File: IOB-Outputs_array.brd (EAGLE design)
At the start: 104.1 x 106.7 mm, 65 parts

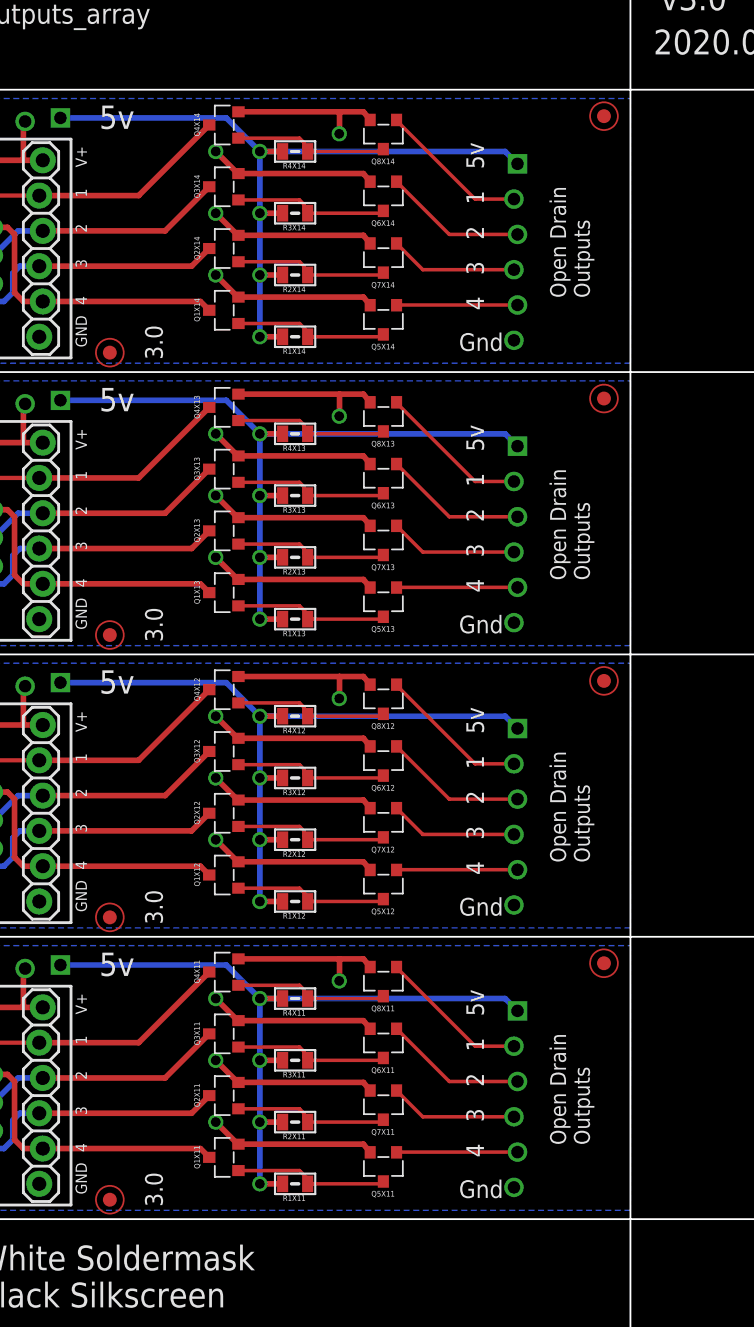
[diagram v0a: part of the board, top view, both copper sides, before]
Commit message: fixed SPCoast.lbr diode orientation
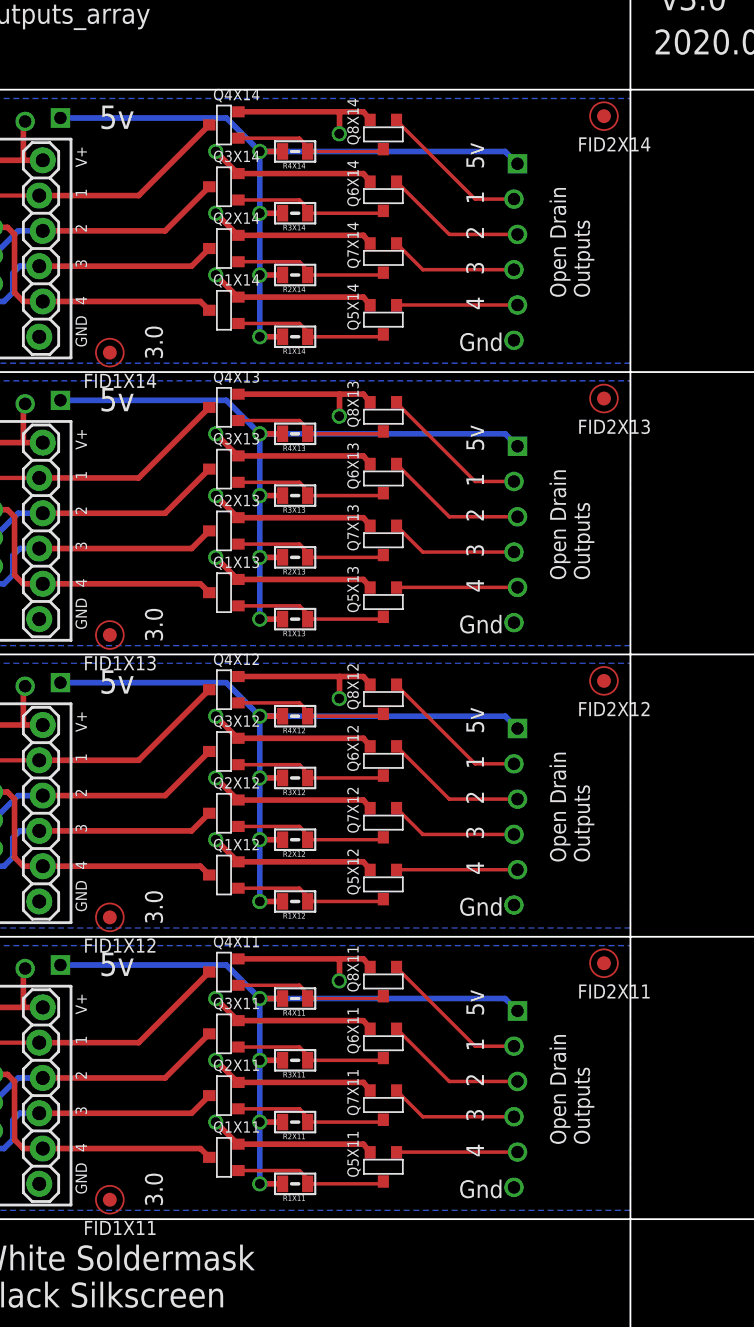
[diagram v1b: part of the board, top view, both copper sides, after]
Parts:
- turned Q1X11 to 0 degrees
- turned Q1X12 to 0 degrees
- turned Q1X13 to 0 degrees
- turned Q1X14 to 0 degrees
- turned Q2X11 to 0 degrees
- turned Q2X12 to 0 degrees
- turned Q2X13 to 0 degrees
- turned Q2X14 to 0 degrees
- turned Q3X11 to 0 degrees
- turned Q3X12 to 0 degrees
- turned Q3X13 to 0 degrees
- turned Q3X14 to 0 degrees
- turned Q4X11 to 0 degrees
- turned Q4X12 to 0 degrees
- turned Q4X13 to 0 degrees
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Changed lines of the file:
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@@
 <element name="FID1X11" library="SPCoast" package="FIDUCIAL_1MM" value="" x="41.275" y="10.287"/>
 <element name="FID2X11" library="SPCoast" package="FIDUCIAL_1MM" value="" x="76.835" y="27.305"/>
-<element name="Q1X11" library="SPCoast" package="SOT23-3" value="" x="49.53" y="13.335" rot="R90"/>
-<element name="Q2X11" library="SPCoast" package="SOT23-3" value="" x="49.53" y="17.78" rot="R90"/>
-<element name="Q3X11" library="SPCoast" package="SOT23-3" value="" x="49.53" y="22.225" rot="R90"/>
-<element name="Q4X11" library="SPCoast" package="SOT23-3" value="" x="49.53" y="26.67" rot="R90"/>
-<element name="Q5X11" library="SPCoast" package="SOT23-3" value="" x="60.96" y="12.7" rot="R180"/>
-<element name="Q6X11" library="SPCoast" package="SOT23-3" value="" x="60.96" y="21.59" rot="R180"/>
-<element name="Q7X11" library="SPCoast" package="SOT23-3" value="" x="60.96" y="17.145" rot="R180"/>
-<element name="Q8X11" library="SPCoast" package="SOT23-3" value="" x="60.96" y="26.035" rot="R180"/>
+<element name="Q1X11" library="SPCoast" package="SOT23-3" value="" x="49.53" y="13.335"/>
+<element name="Q2X11" library="SPCoast" package="SOT23-3" value="" x="49.53" y="17.78"/>
+<element name="Q3X11" library="SPCoast" package="SOT23-3" value="" x="49.53" y="22.225"/>
+<element name="Q4X11" library="SPCoast" package="SOT23-3" value="" x="49.53" y="26.67"/>
+<element name="Q5X11" library="SPCoast" package="SOT23-3" value="" x="60.96" y="12.7" rot="R90"/>
+<element name="Q6X11" library="SPCoast" package="SOT23-3" value="" x="60.96" y="21.59" rot="R90"/>
+<element name="Q7X11" library="SPCoast" package="SOT23-3" value="" x="60.96" y="17.145" rot="R90"/>
+<element name="Q8X11" library="SPCoast" package="SOT23-3" value="" x="60.96" y="26.035" rot="R90"/>
 <element name="R1X11" library="SPCoast" package="0805-RES" value="" x="54.61" y="11.43" rot="R180"/>
 <element name="R2X11" library="SPCoast" package="0805-RES" value="" x="54.61" y="15.875" rot="R180"/>
@@
 <element name="FID1X12" library="SPCoast" package="FIDUCIAL_1MM" value="" x="41.275" y="30.607"/>
 <element name="FID2X12" library="SPCoast" package="FIDUCIAL_1MM" value="" x="76.835" y="47.625"/>
-<element name="Q1X12" library="SPCoast" package="SOT23-3" value="" x="49.53" y="33.655" rot="R90"/>
-<element name="Q2X12" library="SPCoast" package="SOT23-3" value="" x="49.53" y="38.1" rot="R90"/>
-<element name="Q3X12" library="SPCoast" package="SOT23-3" value="" x="49.53" y="42.545" rot="R90"/>
-<element name="Q4X12" library="SPCoast" package="SOT23-3" value="" x="49.53" y="46.99" rot="R90"/>
-<element name="Q5X12" library="SPCoast" package="SOT23-3" value="" x="60.96" y="33.02" rot="R180"/>
-<element name="Q6X12" library="SPCoast" package="SOT23-3" value="" x="60.96" y="41.91" rot="R180"/>
-<element name="Q7X12" library="SPCoast" package="SOT23-3" value="" x="60.96" y="37.465" rot="R180"/>
-<element name="Q8X12" library="SPCoast" package="SOT23-3" value="" x="60.96" y="46.355" rot="R180"/>
+<element name="Q1X12" library="SPCoast" package="SOT23-3" value="" x="49.53" y="33.655"/>
+<element name="Q2X12" library="SPCoast" package="SOT23-3" value="" x="49.53" y="38.1"/>
+<element name="Q3X12" library="SPCoast" package="SOT23-3" value="" x="49.53" y="42.545"/>
+<element name="Q4X12" library="SPCoast" package="SOT23-3" value="" x="49.53" y="46.99"/>
+<element name="Q5X12" library="SPCoast" package="SOT23-3" value="" x="60.96" y="33.02" rot="R90"/>
+<element name="Q6X12" library="SPCoast" package="SOT23-3" value="" x="60.96" y="41.91" rot="R90"/>
+<element name="Q7X12" library="SPCoast" package="SOT23-3" value="" x="60.96" y="37.465" rot="R90"/>
+<element name="Q8X12" library="SPCoast" package="SOT23-3" value="" x="60.96" y="46.355" rot="R90"/>
 <element name="R1X12" library="SPCoast" package="0805-RES" value="" x="54.61" y="31.75" rot="R180"/>
 <element name="R2X12" library="SPCoast" package="0805-RES" value="" x="54.61" y="36.195" rot="R180"/>
@@
 <element name="FID1X13" library="SPCoast" package="FIDUCIAL_1MM" value="" x="41.275" y="50.927"/>
 <element name="FID2X13" library="SPCoast" package="FIDUCIAL_1MM" value="" x="76.835" y="67.945"/>
-<element name="Q1X13" library="SPCoast" package="SOT23-3" value="" x="49.53" y="53.975" rot="R90"/>
-<element name="Q2X13" library="SPCoast" package="SOT23-3" value="" x="49.53" y="58.42" rot="R90"/>
-<element name="Q3X13" library="SPCoast" package="SOT23-3" value="" x="49.53" y="62.865" rot="R90"/>
-<element name="Q4X13" library="SPCoast" package="SOT23-3" value="" x="49.53" y="67.31" rot="R90"/>
-<element name="Q5X13" library="SPCoast" package="SOT23-3" value="" x="60.96" y="53.34" rot="R180"/>
-<element name="Q6X13" library="SPCoast" package="SOT23-3" value="" x="60.96" y="62.23" rot="R180"/>
-<element name="Q7X13" library="SPCoast" package="SOT23-3" value="" x="60.96" y="57.785" rot="R180"/>
-<element name="Q8X13" library="SPCoast" package="SOT23-3" value="" x="60.96" y="66.675" rot="R180"/>
+<element name="Q1X13" library="SPCoast" package="SOT23-3" value="" x="49.53" y="53.975"/>
+<element name="Q2X13" library="SPCoast" package="SOT23-3" value="" x="49.53" y="58.42"/>
+<element name="Q3X13" library="SPCoast" package="SOT23-3" value="" x="49.53" y="62.865"/>
+<element name="Q4X13" library="SPCoast" package="SOT23-3" value="" x="49.53" y="67.31"/>
+<element name="Q5X13" library="SPCoast" package="SOT23-3" value="" x="60.96" y="53.34" rot="R90"/>
+<element name="Q6X13" library="SPCoast" package="SOT23-3" value="" x="60.96" y="62.23" rot="R90"/>
+<element name="Q7X13" library="SPCoast" package="SOT23-3" value="" x="60.96" y="57.785" rot="R90"/>
+<element name="Q8X13" library="SPCoast" package="SOT23-3" value="" x="60.96" y="66.675" rot="R90"/>
 <element name="R1X13" library="SPCoast" package="0805-RES" value="" x="54.61" y="52.07" rot="R180"/>
 <element name="R2X13" library="SPCoast" package="0805-RES" value="" x="54.61" y="56.515" rot="R180"/>
@@
 <element name="FID1X14" library="SPCoast" package="FIDUCIAL_1MM" value="" x="41.275" y="71.247"/>
 <element name="FID2X14" library="SPCoast" package="FIDUCIAL_1MM" value="" x="76.835" y="88.265"/>
-<element name="Q1X14" library="SPCoast" package="SOT23-3" value="" x="49.53" y="74.295" rot="R90"/>
-<element name="Q2X14" library="SPCoast" package="SOT23-3" value="" x="49.53" y="78.74" rot="R90"/>
-<element name="Q3X14" library="SPCoast" package="SOT23-3" value="" x="49.53" y="83.185" rot="R90"/>
-<element name="Q4X14" library="SPCoast" package="SOT23-3" value="" x="49.53" y="87.63" rot="R90"/>
-<element name="Q5X14" library="SPCoast" package="SOT23-3" value="" x="60.96" y="73.66" rot="R180"/>
-<element name="Q6X14" library="SPCoast" package="SOT23-3" value="" x="60.96" y="82.55" rot="R180"/>
-<element name="Q7X14" library="SPCoast" package="SOT23-3" value="" x="60.96" y="78.105" rot="R180"/>
-<element name="Q8X14" library="SPCoast" package="SOT23-3" value="" x="60.96" y="86.995" rot="R180"/>
+<element name="Q1X14" library="SPCoast" package="SOT23-3" value="" x="49.53" y="74.295"/>
+<element name="Q2X14" library="SPCoast" package="SOT23-3" value="" x="49.53" y="78.74"/>
+<element name="Q3X14" library="SPCoast" package="SOT23-3" value="" x="49.53" y="83.185"/>
+<element name="Q4X14" library="SPCoast" package="SOT23-3" value="" x="49.53" y="87.63"/>
+<element name="Q5X14" library="SPCoast" package="SOT23-3" value="" x="60.96" y="73.66" rot="R90"/>
+<element name="Q6X14" library="SPCoast" package="SOT23-3" value="" x="60.96" y="82.55" rot="R90"/>
+<element name="Q7X14" library="SPCoast" package="SOT23-3" value="" x="60.96" y="78.105" rot="R90"/>
+<element name="Q8X14" library="SPCoast" package="SOT23-3" value="" x="60.96" y="86.995" rot="R90"/>
 <element name="R1X14" library="SPCoast" package="0805-RES" value="" x="54.61" y="72.39" rot="R180"/>
 <element name="R2X14" library="SPCoast" package="0805-RES" value="" x="54.61" y="76.835" rot="R180"/>

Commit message: Added missing values
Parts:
- Q1X11, Q1X12, Q1X13, Q1X14, Q2X11, Q2X12, Q2X13, Q2X14, Q3X11, Q3X12, Q3X13, Q3X14, Q4X11, Q4X12, Q4X13, Q4X14, Q5X11, Q5X12, Q5X13, Q5X14, Q6X11, Q6X12, Q6X13, Q6X14, Q7X11, Q7X12, Q7X13, Q7X14, Q8X11, Q8X12, Q8X13, Q8X14: value (none) -> MOSFET-N
- R1X11, R1X12, R1X13, R1X14, R2X11, R2X12, R2X13, R2X14, R3X11, R3X12, R3X13, R3X14, R4X11, R4X12, R4X13, R4X14: value (none) -> 10k

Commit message: normalized silkscreen layout across IOBs
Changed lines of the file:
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@@
 <plain>
 <text x="27.94" y="14.351" size="1.27" layer="21" font="vector" rot="R90">IO4-IOB</text>
-<text x="45.085" y="9.779" size="1.27" layer="21" font="vector" rot="R90">3.0</text>
+<text x="77.47" y="9.779" size="1.27" layer="21" font="vector" rot="R90">3.0</text>
 <text x="75.819" y="14.224" size="1.143" layer="21" font="vector" rot="R90">Open Drain
 Outputs</text>
@@
 <text x="55.626" y="26.9875" size="1.016" layer="125" font="vector" rot="R180">R4</text>
 <text x="27.94" y="34.671" size="1.27" layer="21" font="vector" rot="R90">IO4-IOB</text>
-<text x="45.085" y="30.099" size="1.27" layer="21" font="vector" rot="R90">3.0</text>
+<text x="77.47" y="30.099" size="1.27" layer="21" font="vector" rot="R90">3.0</text>
 <text x="75.819" y="34.544" size="1.143" layer="21" font="vector" rot="R90">Open Drain
 Outputs</text>
@@
 <text x="55.626" y="47.3075" size="1.016" layer="125" font="vector" rot="R180">R4</text>
 <text x="27.94" y="54.991" size="1.27" layer="21" font="vector" rot="R90">IO4-IOB</text>
-<text x="45.085" y="50.419" size="1.27" layer="21" font="vector" rot="R90">3.0</text>
+<text x="77.47" y="50.419" size="1.27" layer="21" font="vector" rot="R90">3.0</text>
 <text x="75.819" y="54.864" size="1.143" layer="21" font="vector" rot="R90">Open Drain
 Outputs</text>
@@
 <text x="55.626" y="67.6275" size="1.016" layer="125" font="vector" rot="R180">R4</text>
 <text x="27.94" y="75.311" size="1.27" layer="21" font="vector" rot="R90">IO4-IOB</text>
-<text x="45.085" y="70.739" size="1.27" layer="21" font="vector" rot="R90">3.0</text>
+<text x="77.47" y="70.739" size="1.27" layer="21" font="vector" rot="R90">3.0</text>
 <text x="75.819" y="75.184" size="1.143" layer="21" font="vector" rot="R90">Open Drain
 Outputs</text>

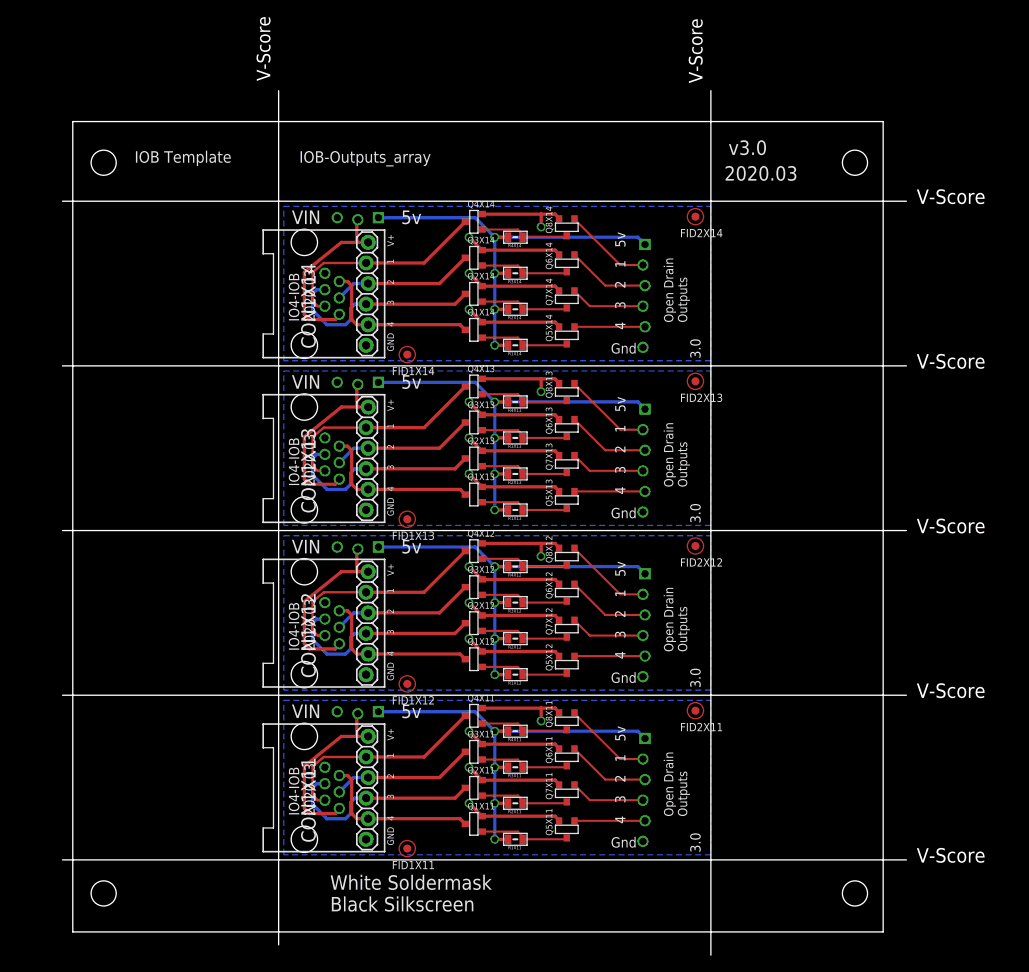
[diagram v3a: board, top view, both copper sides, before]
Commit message: move text from DOCU to TPLACE
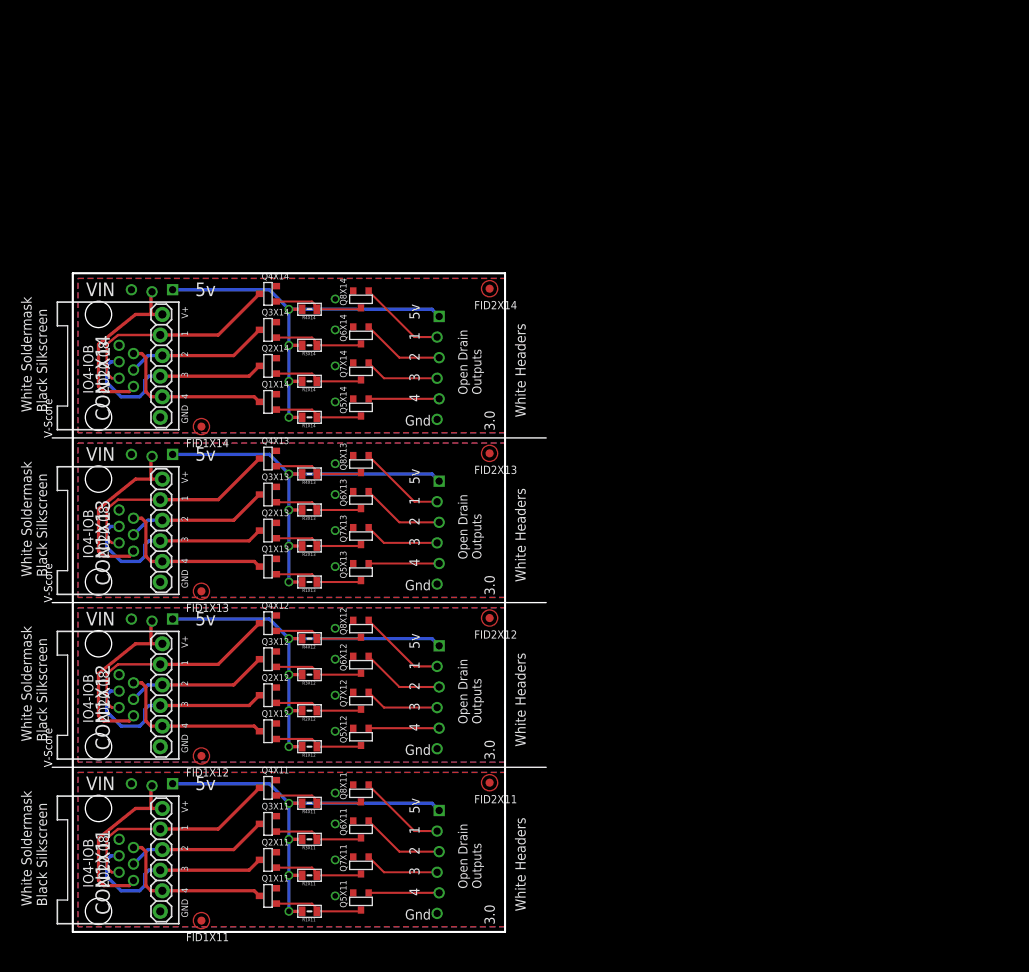
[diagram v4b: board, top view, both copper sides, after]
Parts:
- removed U$1X1: (no value), SPCoast:BOARD-DINRAIL-3.17IN-H4X-IOB
- FID1X11, FID1X12, FID1X13, FID1X14, FID2X11, FID2X12, FID2X13, FID2X14: value (none) -> FIDUCIAL
- U$1X11, U$1X12, U$1X13, U$1X14: value (none) -> CONNECTOR-IO4-IOBFULL
- moved Q1X11 26.9 mm to (24.1, 4.45)
- moved Q1X12 26.9 mm to (24.1, 24.8)
- moved Q1X13 26.9 mm to (24.1, 45.1)
- moved Q1X14 26.9 mm to (24.1, 65.4)
- moved Q2X11 26.9 mm to (24.1, 8.89)
- moved Q2X12 26.9 mm to (24.1, 29.2)
- moved Q2X13 26.9 mm to (24.1, 49.5)
- moved Q2X14 26.9 mm to (24.1, 69.8)
- moved Q3X11 26.9 mm to (24.1, 13.3)
- moved Q3X12 26.9 mm to (24.1, 33.7)
- moved Q3X13 26.9 mm to (24.1, 54.0)
- moved Q3X14 26.9 mm to (24.1, 74.3)
- moved Q4X11 26.9 mm to (24.1, 17.8)
- moved Q4X12 26.9 mm to (24.1, 38.1)
- moved Q4X13 26.9 mm to (24.1, 58.4)
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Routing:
- net GNDX13: track 47.5 -> 0.13 mm
- net GNDX11: track 47.5 -> 0.13 mm
- net GNDX14: track 47.5 -> 0.13 mm
- net GNDX12: track 47.5 -> 0.13 mm
- added copper zone on layer 1, net GNDX11
- added copper zone on layer 1, net GNDX12
- added copper zone on layer 1, net GNDX13
- added copper zone on layer 1, net GNDX14
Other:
- board size 104.1 x 106.7 mm -> 61 x 81.3 mm
- board text added: "2020.08"
- board text added: "FID1"
- board text added: "FID2"
- board text added: "V-Score"
- board text added: "White Headers"
- board text removed: "2020.03"
- board text removed: "v3.0"
